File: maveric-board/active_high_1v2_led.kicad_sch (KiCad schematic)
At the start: 4 parts, among them Q2 DMN2005K-7

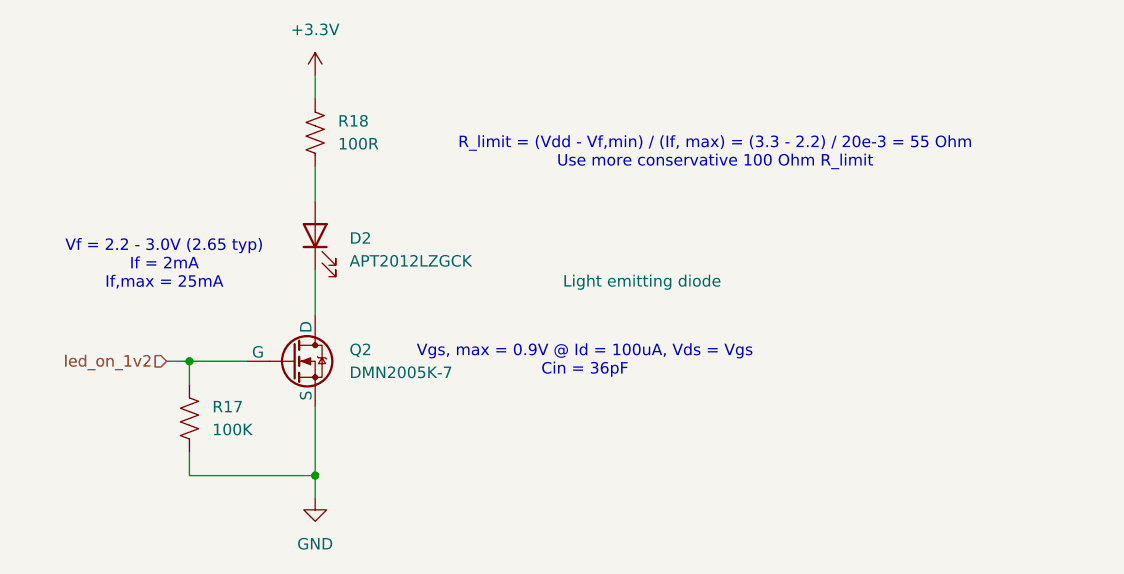
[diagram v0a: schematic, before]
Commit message: add mfr part # attribute to each symbol, resync board layout, remove excess VDDV decap
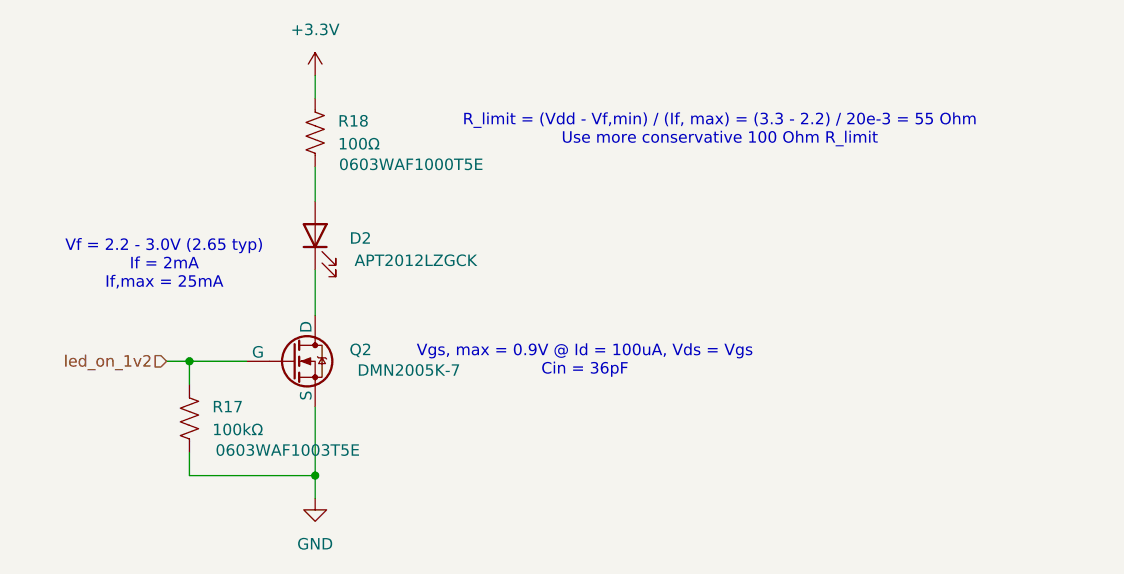
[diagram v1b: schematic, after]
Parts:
- D2: value APT2012LZGCK -> ~; Mfr Part # (none) -> APT2012LZGCK
- Q2: value DMN2005K-7 -> ~; Mfr Part # (none) -> DMN2005K-7
- R17: value 100K -> 100kΩ; Mfr Part # (none) -> 0603WAF1003T5E
- R18: value 100R -> 100Ω; Mfr Part # (none) -> 0603WAF1000T5E
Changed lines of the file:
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@@
 	(text "R_limit = (Vdd - Vf,min) / (If, max) = (3.3 - 2.2) / 20e-3 = 55 Ohm\nUse more conservative 100 Ohm R_limit"
 		(exclude_from_sim no)
-		(at 90.17 30.226 0)
+		(at 90.678 27.686 0)
 		(effects
 			(font
@@
 		(on_board yes)
 		(dnp no)
-		(fields_autoplaced yes)
 		(property "Reference" "Q2"
 			(at 49.53 52.0699 0)
@@
 			)
 		)
-		(property "Value" "DMN2005K-7"
+		(property "Value" "~"
 			(at 49.53 54.6099 0)
 			(effects
@@
 			)
 		)
-		(property "Datasheet" "https://ngspice.sourceforge.io/docs/ngspice-html-manual/manual.xhtml#cha_MOSFETs"
+		(property "Datasheet" ""
 			(at 43.18 66.04 0)
 			(effects
@@
 				)
 				(hide yes)
+			)
+		)
+		(property "Mfr Part #" "DMN2005K-7"
+			(at 56.134 54.356 0)
+			(effects
+				(font
+					(size 1.27 1.27)
+				)
 			)
 		)
@@
 		(on_board yes)
 		(dnp no)
-		(fields_autoplaced yes)
 		(property "Reference" "R18"
 			(at 48.26 26.6699 0)
@@
 			)
 		)
-		(property "Value" "100R"
+		(property "Value" "100Ω"
 			(at 48.26 29.2099 0)
 			(effects
@@
 			)
 		)
-		(property "Datasheet" "~"
+		(property "Datasheet" ""
 			(at 45.72 27.94 0)
 			(effects
@@
 				)
 				(hide yes)
+			)
+		)
+		(property "Mfr Part #" "0603WAF1000T5E"
+			(at 56.388 31.496 0)
+			(effects
+				(font
+					(size 1.27 1.27)
+				)
 			)
 		)
@@
 		(on_board yes)
 		(dnp no)
-		(fields_autoplaced yes)
 		(property "Reference" "R17"
 			(at 34.29 58.4199 0)
@@
 			)
 		)
-		(property "Value" "100K"
+		(property "Value" "100kΩ"
 			(at 34.29 60.9599 0)
 			(effects
@@
 			)
 		)
-		(property "Datasheet" "~"
+		(property "Datasheet" ""
 			(at 31.75 59.69 0)
 			(effects
@@
 				)
 				(hide yes)
+			)
+		)
+		(property "Mfr Part #" "0603WAF1003T5E"
+			(at 42.672 63.246 0)
+			(effects
+				(font
+					(size 1.27 1.27)
+				)
 			)
 		)
@@
 			)
 		)
-		(property "Value" "APT2012LZGCK"
+		(property "Value" "~"
 			(at 49.53 42.2274 90)
 			(effects
@@
 			)
 		)
-		(property "Datasheet" "~"
+		(property "Datasheet" ""
 			(at 45.72 39.37 0)
 			(effects
@@
 					(size 1.27 1.27)
 				)
+				(hide yes)
 			)
 		)
@@
 			)
 		)
+		(property "Mfr Part #" "APT2012LZGCK"
+			(at 56.896 42.164 90)
+			(effects
+				(font
+					(size 1.27 1.27)
+				)
+			)
+		)

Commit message: resync all symbols to schematic, reannotate schematic
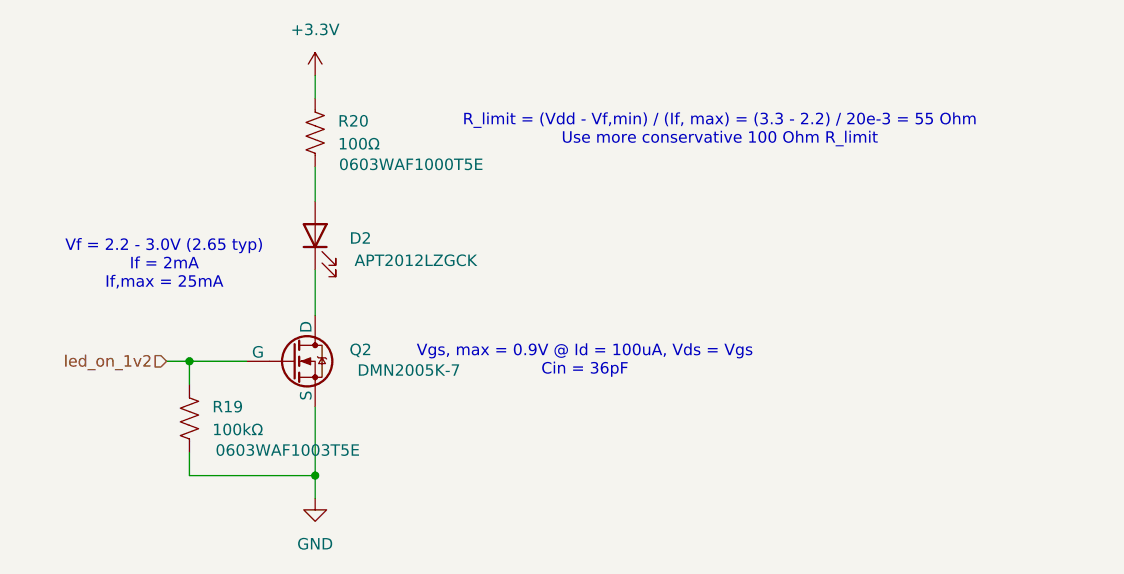
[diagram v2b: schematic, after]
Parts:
- renumbered R17 to R19, R18 to R20
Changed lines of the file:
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@@
 		(dnp no)
 		(fields_autoplaced yes)
-		(property "Reference" "#PWR0111"
+		(property "Reference" "#PWR0116"
 			(at 45.72 74.93 0)
 			(effects
@@
 			(project "maveric-board"
 				(path "/ae861d46-65fb-4872-932f-ad48addb0154/04d5a329-5af7-4fa0-b263-ed8b9ef94f0b"
-					(reference "#PWR0111")
+					(reference "#PWR0116")
 					(unit 1)
 				)
 				(path "/ae861d46-65fb-4872-932f-ad48addb0154/07de628d-3b41-4acd-98a7-6b7c73c5b4dd"
-					(reference "#PWR0113")
+					(reference "#PWR0118")
 					(unit 1)
 				)
 				(path "/ae861d46-65fb-4872-932f-ad48addb0154/482467b2-b94e-4ec7-a3c4-312d002b6711"
-					(reference "#PWR0115")
+					(reference "#PWR0120")
 					(unit 1)
 				)
 				(path "/ae861d46-65fb-4872-932f-ad48addb0154/9dce5c8c-15df-41df-971c-7c9355dface0"
-					(reference "#PWR0109")
+					(reference "#PWR0114")
 					(unit 1)
 				)
 				(path "/ae861d46-65fb-4872-932f-ad48addb0154/d720b503-5d41-4e8c-a69b-3a22cbc341eb"
-					(reference "#PWR0117")
+					(reference "#PWR0122")
 					(unit 1)
 				)
@@
 			)
 		)
-		(property "Datasheet" ""
+		(property "Datasheet" "https://ngspice.sourceforge.io/docs/ngspice-html-manual/manual.xhtml#cha_MOSFETs"
 			(at 43.18 66.04 0)
 			(effects
@@
 		(on_board yes)
 		(dnp no)
-		(property "Reference" "R18"
+		(property "Reference" "R20"
 			(at 48.26 26.6699 0)
 			(effects
@@
 			)
 		)
-		(property "Datasheet" ""
+		(property "Datasheet" "~"
 			(at 45.72 27.94 0)
 			(effects
@@
 			(project "maveric-board"
 				(path "/ae861d46-65fb-4872-932f-ad48addb0154/04d5a329-5af7-4fa0-b263-ed8b9ef94f0b"
+					(reference "R20")
+					(unit 1)
+				)
+				(path "/ae861d46-65fb-4872-932f-ad48addb0154/07de628d-3b41-4acd-98a7-6b7c73c5b4dd"
+					(reference "R22")
+					(unit 1)
+				)
+				(path "/ae861d46-65fb-4872-932f-ad48addb0154/482467b2-b94e-4ec7-a3c4-312d002b6711"
+					(reference "R24")
+					(unit 1)
+				)
+				(path "/ae861d46-65fb-4872-932f-ad48addb0154/9dce5c8c-15df-41df-971c-7c9355dface0"
 					(reference "R18")
 					(unit 1)
 				)
-				(path "/ae861d46-65fb-4872-932f-ad48addb0154/07de628d-3b41-4acd-98a7-6b7c73c5b4dd"
-					(reference "R20")
-					(unit 1)
-				)
-				(path "/ae861d46-65fb-4872-932f-ad48addb0154/482467b2-b94e-4ec7-a3c4-312d002b6711"
-					(reference "R22")
-					(unit 1)
-				)
-				(path "/ae861d46-65fb-4872-932f-ad48addb0154/9dce5c8c-15df-41df-971c-7c9355dface0"
-					(reference "R16")
-					(unit 1)
-				)
 				(path "/ae861d46-65fb-4872-932f-ad48addb0154/d720b503-5d41-4e8c-a69b-3a22cbc341eb"
-					(reference "R24")
+					(reference "R26")
 					(unit 1)
 				)
@@
 		(dnp no)
 		(fields_autoplaced yes)
-		(property "Reference" "#PWR0110"
+		(property "Reference" "#PWR0115"
 			(at 45.72 25.4 0)
 			(effects
@@
 			(project ""
 				(path "/ae861d46-65fb-4872-932f-ad48addb0154/04d5a329-5af7-4fa0-b263-ed8b9ef94f0b"
-					(reference "#PWR0110")
+					(reference "#PWR0115")
 					(unit 1)
 				)
 				(path "/ae861d46-65fb-4872-932f-ad48addb0154/07de628d-3b41-4acd-98a7-6b7c73c5b4dd"
-					(reference "#PWR0112")
+					(reference "#PWR0117")
 					(unit 1)
 				)
 				(path "/ae861d46-65fb-4872-932f-ad48addb0154/482467b2-b94e-4ec7-a3c4-312d002b6711"
-					(reference "#PWR0114")
+					(reference "#PWR0119")
 					(unit 1)
 				)
 				(path "/ae861d46-65fb-4872-932f-ad48addb0154/9dce5c8c-15df-41df-971c-7c9355dface0"
-					(reference "#PWR0108")
+					(reference "#PWR0113")
 					(unit 1)
 				)
 				(path "/ae861d46-65fb-4872-932f-ad48addb0154/d720b503-5d41-4e8c-a69b-3a22cbc341eb"
-					(reference "#PWR0116")
+					(reference "#PWR0121")
 					(unit 1)
 				)
@@
 		(on_board yes)
 		(dnp no)
-		(property "Reference" "R17"
+		(property "Reference" "R19"
 			(at 34.29 58.4199 0)
 			(effects
@@
 			)
 		)
-		(property "Datasheet" ""
+		(property "Datasheet" "~"
 			(at 31.75 59.69 0)
 			(effects
@@
 			(project "maveric-board"
 				(path "/ae861d46-65fb-4872-932f-ad48addb0154/04d5a329-5af7-4fa0-b263-ed8b9ef94f0b"
+					(reference "R19")
+					(unit 1)
+				)
+				(path "/ae861d46-65fb-4872-932f-ad48addb0154/07de628d-3b41-4acd-98a7-6b7c73c5b4dd"
+					(reference "R21")
+					(unit 1)
+				)
+				(path "/ae861d46-65fb-4872-932f-ad48addb0154/482467b2-b94e-4ec7-a3c4-312d002b6711"
+					(reference "R23")
+					(unit 1)
+				)
+				(path "/ae861d46-65fb-4872-932f-ad48addb0154/9dce5c8c-15df-41df-971c-7c9355dface0"
 					(reference "R17")
 					(unit 1)
 				)
-				(path "/ae861d46-65fb-4872-932f-ad48addb0154/07de628d-3b41-4acd-98a7-6b7c73c5b4dd"
-					(reference "R19")
-					(unit 1)
-				)
-				(path "/ae861d46-65fb-4872-932f-ad48addb0154/482467b2-b94e-4ec7-a3c4-312d002b6711"
-					(reference "R21")
-					(unit 1)
-				)
-				(path "/ae861d46-65fb-4872-932f-ad48addb0154/9dce5c8c-15df-41df-971c-7c9355dface0"
-					(reference "R15")
-					(unit 1)
-				)
 				(path "/ae861d46-65fb-4872-932f-ad48addb0154/d720b503-5d41-4e8c-a69b-3a22cbc341eb"
-					(reference "R23")
+					(reference "R25")
 					(unit 1)
 				)
@@
 			)
 		)
-		(property "Datasheet" ""
+		(property "Datasheet" "~"
 			(at 45.72 39.37 0)
 			(effects

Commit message: fixup schematic + redo banana jack footprints to match jlc render
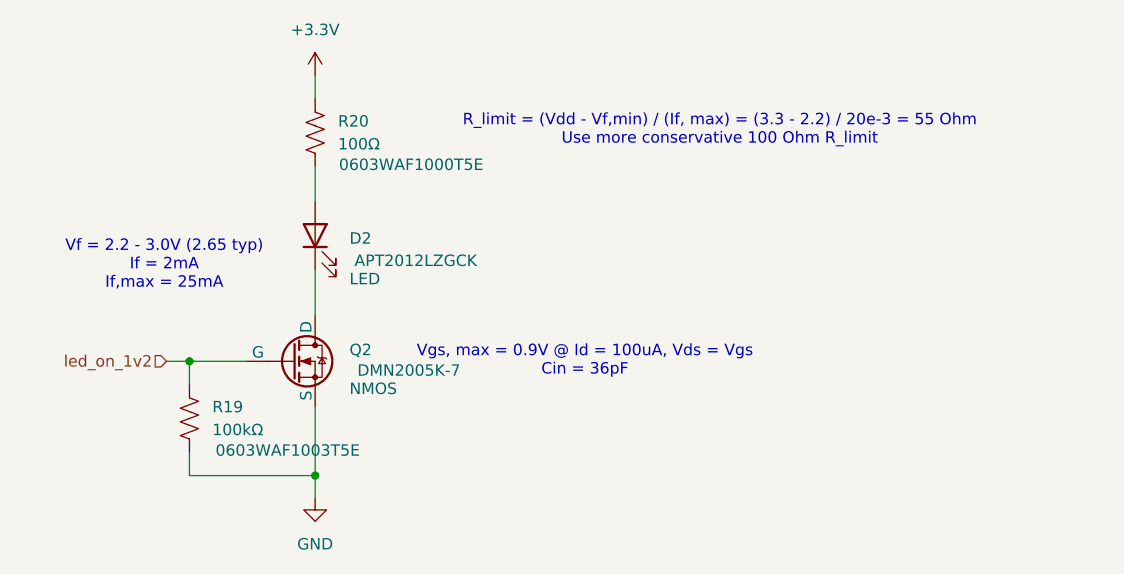
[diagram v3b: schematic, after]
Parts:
- D2: value ~ -> LED
- Q2: value ~ -> NMOS
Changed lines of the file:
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@@
 			)
 		)
-		(property "Value" "~"
-			(at 49.53 54.6099 0)
+		(property "Value" "NMOS"
+			(at 49.53 56.388 0)
 			(effects
 				(font
@@
 			)
 		)
-		(property "Value" "~"
-			(at 49.53 42.2274 90)
-			(effects
-				(font
+		(property "Value" "LED"
+			(at 49.53 44.196 90)
+			(effects
+				(font
